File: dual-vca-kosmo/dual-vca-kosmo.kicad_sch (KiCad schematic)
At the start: 74 parts, among them J1 Conn_02x05_Odd_Even, J10 in2, J11 Conn_02x05_Odd_Even, J2 Conn_02x05_Odd_Even, J3 cv1, J4 cv2, J5 cvdual, J6 mixout, J7 out1, J8 out2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

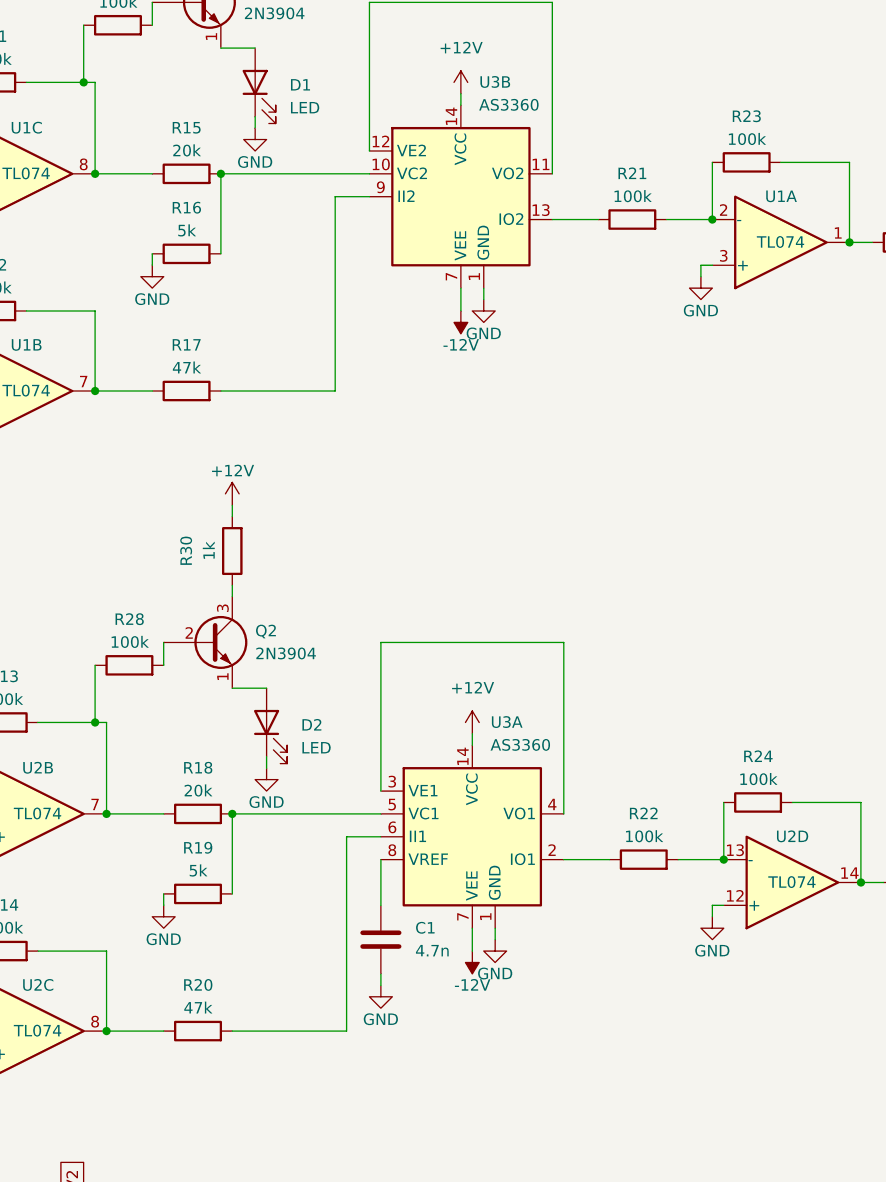
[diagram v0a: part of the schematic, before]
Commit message: Actually update schematic to V1.0
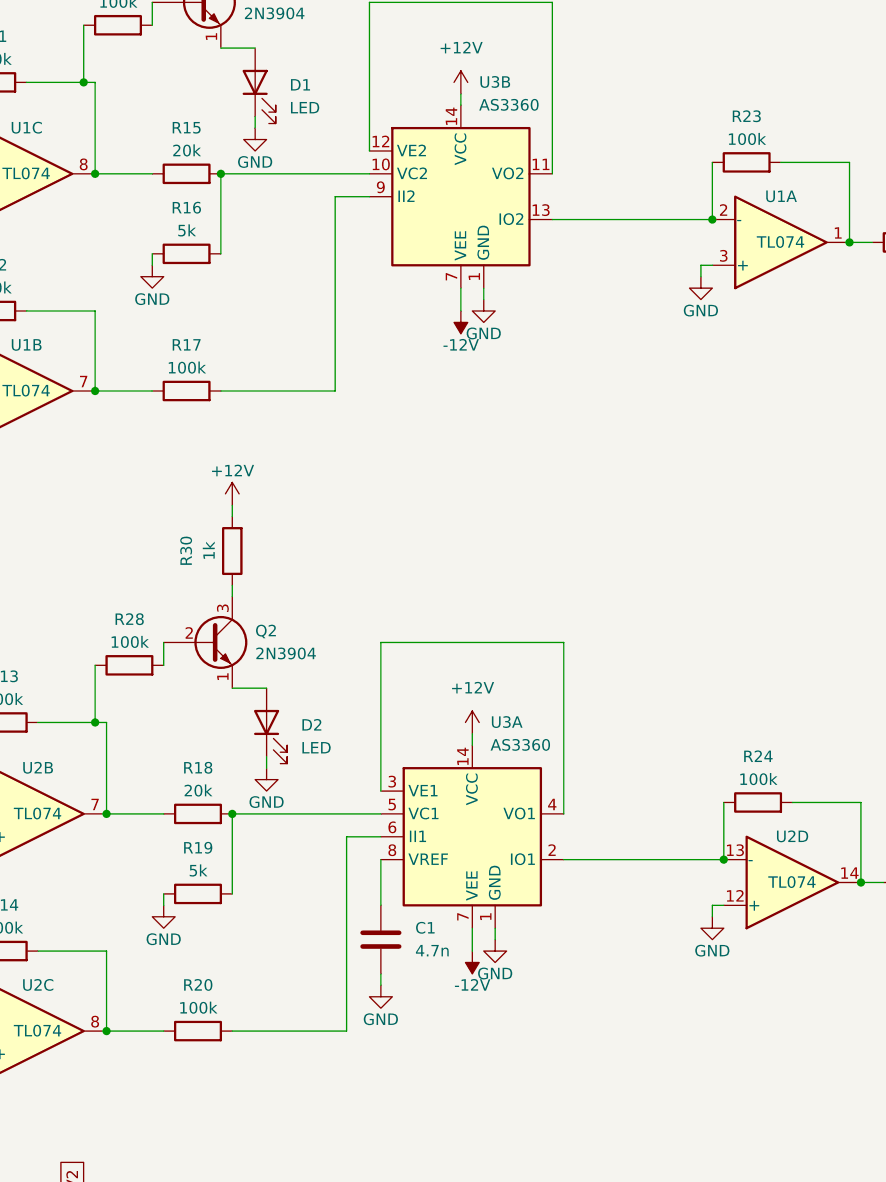
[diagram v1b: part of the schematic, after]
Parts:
- removed R21, R22: 100k, omat:Omaresistor2, symbol Device:R
- R17, R20: value 47k -> 100k
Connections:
- net at R23.1, U1.2 (-): now also U3.13 (IO2)
- net at R24.1, U2.13 (-): now also U3.2 (IO1)

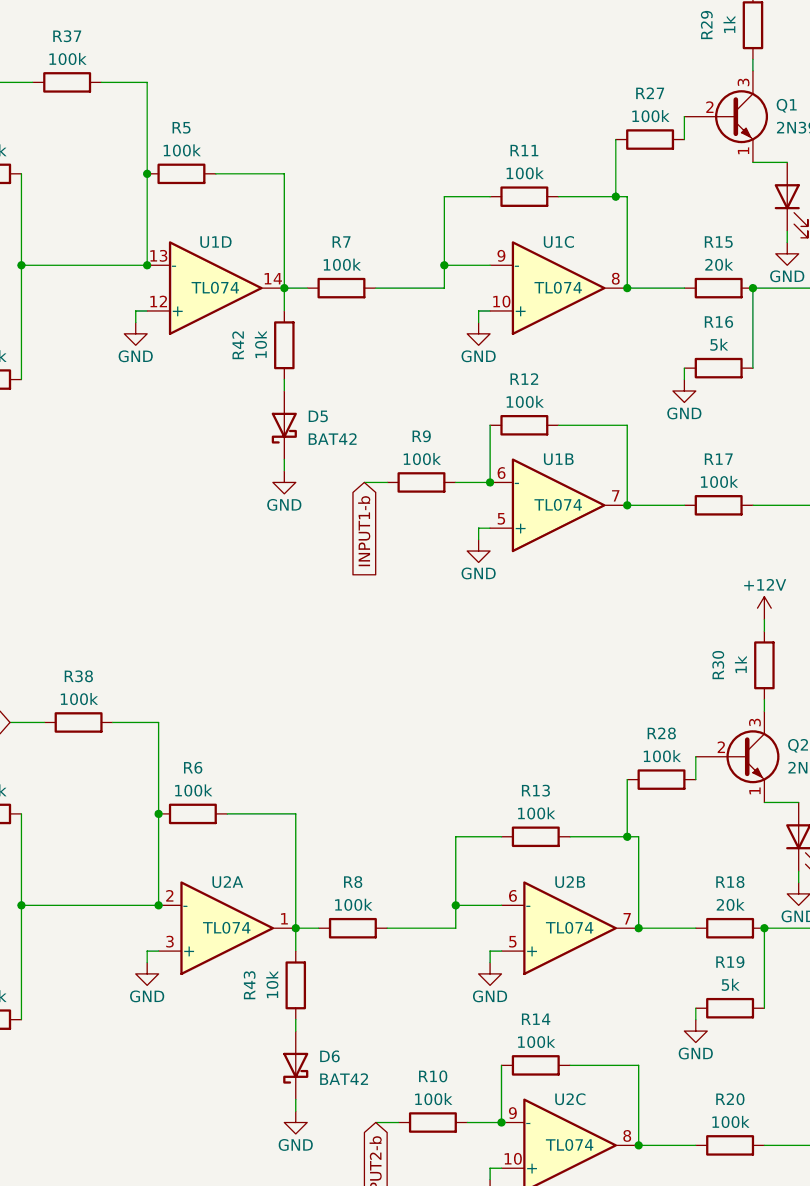
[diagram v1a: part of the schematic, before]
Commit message: Schematic V1.1, fixed CV limiting
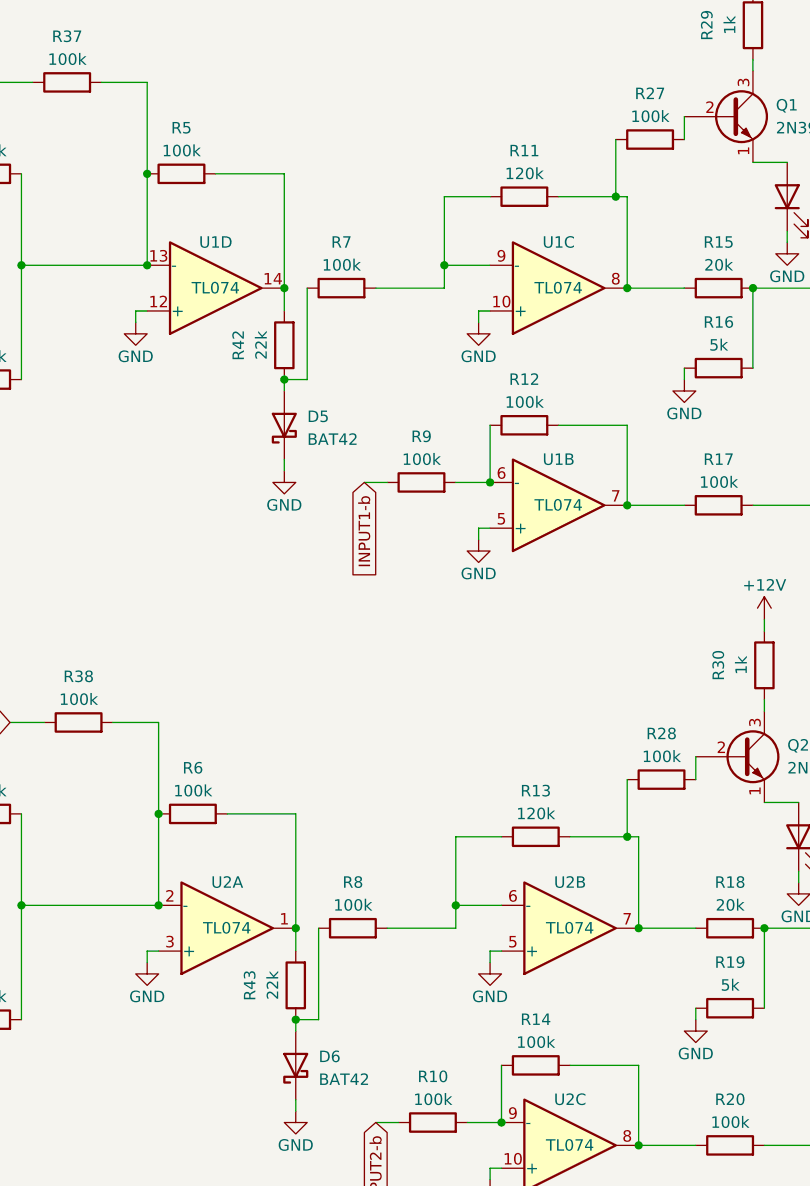
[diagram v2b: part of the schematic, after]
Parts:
- R11, R13: value 100k -> 120k
- R42, R43: value 10k -> 22k
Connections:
- net at D6.2 (A), R43.1: now also R8.1
- net at R43.2, R6.2, U2.1: no longer R8.1
- net at R42.2, R5.2, U1.14: no longer R7.1
- net at D5.2 (A), R42.1: now also R7.1
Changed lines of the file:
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@@
   (title_block
     (title "Krakenpine Kosmo Dual VCA")
-    (rev "1.0")
+    (rev "1.1")
   )
   (junction (at 100.33 78.74) (diameter 0) (color 0 0 0 0)
@@
   (junction (at 292.1 86.36) (diameter 0) (color 0 0 0 0)
   )
+  (junction (at 78.74 138.43) (diameter 0) (color 0 0 0 0)
+  )
   (junction (at 179.07 199.39) (diameter 0) (color 0 0 0 0)
   )
@@
   (junction (at 48.26 125.73) (diameter 0) (color 0 0 0 0)
   )
+  (junction (at 77.47 67.31) (diameter 0) (color 0 0 0 0)
+  )
   (junction (at 195.58 214.63) (diameter 0) (color 0 0 0 0)
   )
@@
   (junction (at 97.79 179.07) (diameter 0) (color 0 0 0 0)
   )
-  (wire (pts (xy 78.74 128.27) (xy 81.28 128.27))
-    (stroke (width 0) (type default))
-  )
   (wire (pts (xy 54.61 212.09) (xy 62.23 212.09))
     (stroke (width 0) (type default))
@@
     (stroke (width 0) (type default))
   )
+  (wire (pts (xy 80.01 67.31) (xy 77.47 67.31))
+    (stroke (width 0) (type default))
+  )
   (wire (pts (xy 157.48 140.97) (xy 157.48 143.51))
     (stroke (width 0) (type default))
@@
     (stroke (width 0) (type default))
   )
+  (wire (pts (xy 80.01 57.15) (xy 80.01 67.31))
+    (stroke (width 0) (type default))
+  )
   (wire (pts (xy 77.47 57.15) (xy 77.47 59.69))
     (stroke (width 0) (type default))
@@
     (stroke (width 0) (type default))
   )
+  (wire (pts (xy 81.28 138.43) (xy 78.74 138.43))
+    (stroke (width 0) (type default))
+  )
   (wire (pts (xy 81.28 179.07) (xy 86.36 179.07))
     (stroke (width 0) (type default))
@@
     (stroke (width 0) (type default))
   )
-  (wire (pts (xy 77.47 57.15) (xy 80.01 57.15))
-    (stroke (width 0) (type default))
-  )
   (wire (pts (xy 96.52 118.11) (xy 96.52 125.73))
     (stroke (width 0) (type default))
@@
     (stroke (width 0) (type default))
   )
+  (wire (pts (xy 81.28 128.27) (xy 81.28 138.43))
+    (stroke (width 0) (type default))
+  )
   (wire (pts (xy 123.19 109.22) (xy 123.19 111.76))
     (stroke (width 0) (type default))
@@
       (effects (font (size 1.27 1.27)))
     )
-    (property "Value" "10k" (at 76.2 134.62 90)
+    (property "Value" "22k" (at 76.2 134.62 90)
       (effects (font (size 1.27 1.27)))
     )
@@
       (effects (font (size 1.27 1.27)))
     )
-    (property "Value" "100k" (at 104.14 44.45 90)
+    (property "Value" "120k" (at 104.14 44.45 90)
       (effects (font (size 1.27 1.27)))
     )
@@
       (effects (font (size 1.27 1.27)))
     )
-    (property "Value" "100k" (at 105.41 115.57 90)
+    (property "Value" "120k" (at 105.41 115.57 90)
       (effects (font (size 1.27 1.27)))
     )
@@
       (effects (font (size 1.27 1.27)))
     )
-    (property "Value" "10k" (at 74.93 63.5 90)
+    (property "Value" "22k" (at 74.93 63.5 90)
       (effects (font (size 1.27 1.27)))
     )
